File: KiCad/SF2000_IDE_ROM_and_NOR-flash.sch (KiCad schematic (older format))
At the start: 7 parts, among them J5 IDE_ATA_44pin, U13 SST39LF040, U14 SST39LF802C, U15 74LVC245A, U16 74LVC245A, U17 74LVC245A

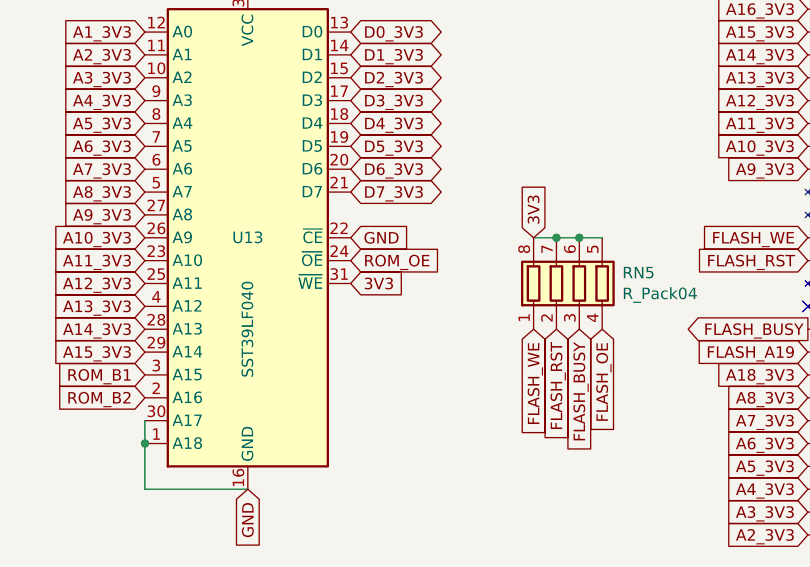
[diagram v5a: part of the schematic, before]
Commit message: added ROM_WE signal/pin to FPGA, removed XRDY-signal/pin, and some silkscreen fixes
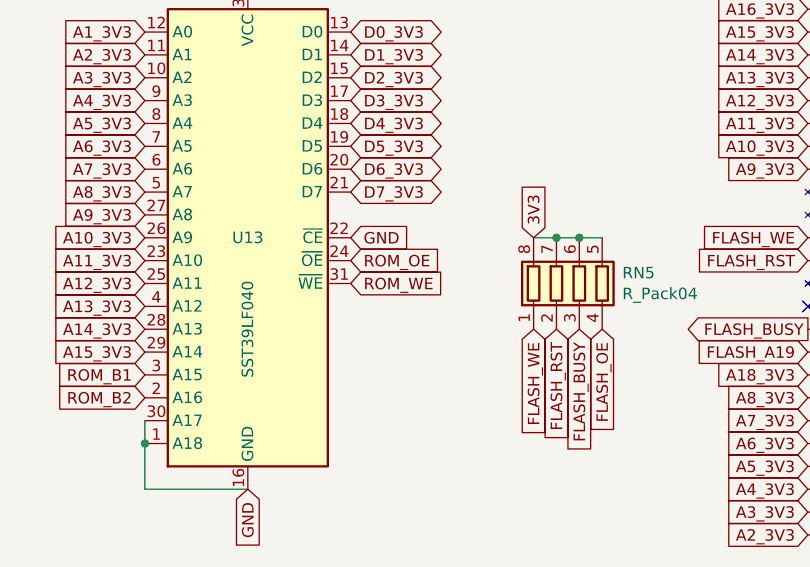
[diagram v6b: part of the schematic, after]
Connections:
- net 3V3: no longer U13.31 (~WE)
- new net ROM_WE: U13.31 (~WE)
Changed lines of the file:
@@
 Wire Wire Line
 	5650 3500 5650 3400
-Text GLabel 6550 2800 2    50   Input ~ 0
-3V3
 NoConn ~ 8550 2900
 $Comp
@@
 Text GLabel 7650 3000 3    50   Input ~ 0
 FLASH_OE
+Text GLabel 6550 2800 2    50   Input ~ 0
+ROM_WE
 $EndSCHEMATC

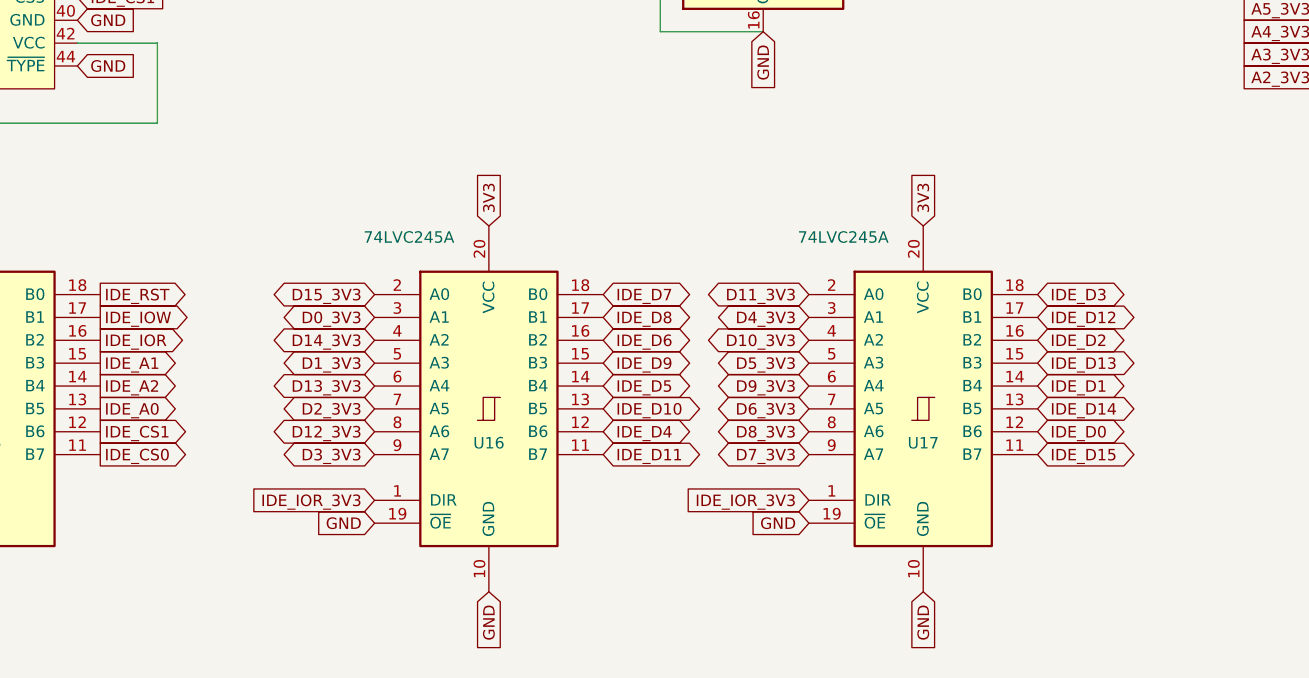
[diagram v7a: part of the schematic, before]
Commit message: added decoupling capacitor for Crystal Oscillator (X1), and some silkcreen fixes/labeling
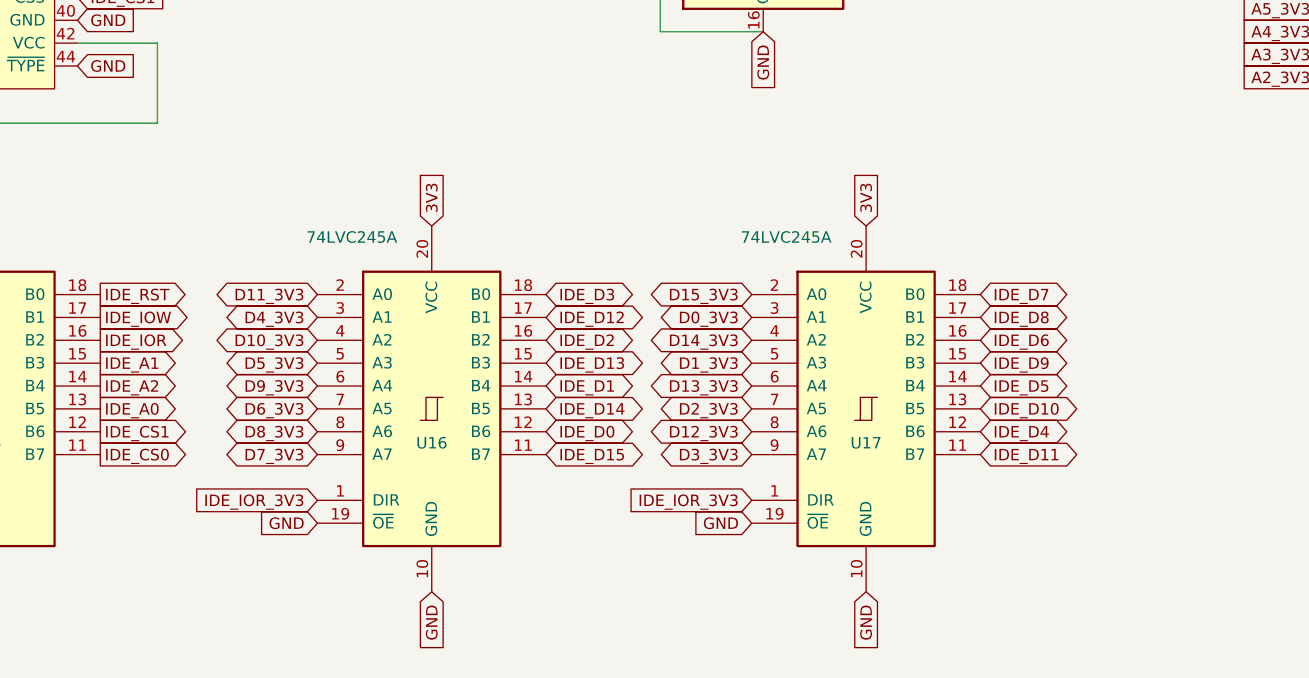
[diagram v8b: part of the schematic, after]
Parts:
- renumbered U17 to U16, U16 to U17
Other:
- moved on the sheet: U16, U17
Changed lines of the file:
@@
 Text GLabel 6550 2400 2    50   BiDi ~ 0
 D7_3V3
-Text GLabel 4400 4950 0    50   BiDi ~ 0
+Text GLabel 6050 4950 0    50   BiDi ~ 0
 D0_3V3
-Text GLabel 4400 5150 0    50   BiDi ~ 0
+Text GLabel 6050 5150 0    50   BiDi ~ 0
 D1_3V3
-Text GLabel 4400 5350 0    50   BiDi ~ 0
+Text GLabel 6050 5350 0    50   BiDi ~ 0
 D2_3V3
-Text GLabel 4400 5550 0    50   BiDi ~ 0
+Text GLabel 6050 5550 0    50   BiDi ~ 0
 D3_3V3
-Text GLabel 6300 4950 0    50   BiDi ~ 0
+Text GLabel 4150 4950 0    50   BiDi ~ 0
 D4_3V3
-Text GLabel 6300 5150 0    50   BiDi ~ 0
+Text GLabel 4150 5150 0    50   BiDi ~ 0
 D5_3V3
-Text GLabel 6300 5350 0    50   BiDi ~ 0
+Text GLabel 4150 5350 0    50   BiDi ~ 0
 D6_3V3
-Text GLabel 6300 5550 0    50   BiDi ~ 0
+Text GLabel 4150 5550 0    50   BiDi ~ 0
 D7_3V3
-Text GLabel 6300 5450 0    50   BiDi ~ 0
+Text GLabel 4150 5450 0    50   BiDi ~ 0
 D8_3V3
-Text GLabel 6300 5250 0    50   BiDi ~ 0
+Text GLabel 4150 5250 0    50   BiDi ~ 0
 D9_3V3
-Text GLabel 6300 5050 0    50   BiDi ~ 0
+Text GLabel 4150 5050 0    50   BiDi ~ 0
 D10_3V3
-Text GLabel 6300 4850 0    50   BiDi ~ 0
+Text GLabel 4150 4850 0    50   BiDi ~ 0
 D11_3V3
-Text GLabel 4400 5450 0    50   BiDi ~ 0
+Text GLabel 6050 5450 0    50   BiDi ~ 0
 D12_3V3
-Text GLabel 4400 5250 0    50   BiDi ~ 0
+Text GLabel 6050 5250 0    50   BiDi ~ 0
 D13_3V3
-Text GLabel 4400 5050 0    50   BiDi ~ 0
+Text GLabel 6050 5050 0    50   BiDi ~ 0
 D14_3V3
-Text GLabel 4400 4850 0    50   BiDi ~ 0
+Text GLabel 6050 4850 0    50   BiDi ~ 0
 D15_3V3
 Text GLabel 2200 4850 0    50   Input ~ 0
@@
 IDE_CS0
 $Comp
-L SF2000:74LVC245A U16
+L SF2000:74LVC245A U17
 U 1 1 628E9EE2
-P 4900 5350
-F 0 "U16" H 4900 5200 50  0000 C CNN
-F 1 "74LVC245A" H 4550 6100 50  0000 C CNN
-F 2 "Package_SO:TSSOP-20_4.4x6.5mm_P0.65mm" H 4900 5350 50  0001 C CNN
-F 3 "http://www.ti.com/lit/gpn/sn74HC245" H 4900 5350 50  0001 C CNN
-	1    4900 5350
+P 6550 5350
+F 0 "U17" H 6550 5200 50  0000 C CNN
+F 1 "74LVC245A" H 6200 6100 50  0000 C CNN
+F 2 "Package_SO:TSSOP-20_4.4x6.5mm_P0.65mm" H 6550 5350 50  0001 C CNN
+F 3 "http://www.ti.com/lit/gpn/sn74HC245" H 6550 5350 50  0001 C CNN
+	1    6550 5350
 	1    0    0    -1
 $EndComp
-Text GLabel 4900 4550 1    50   Input ~ 0
-3V3
-Text GLabel 4900 6150 3    50   Input ~ 0
-GND
-Text GLabel 4400 5850 0    50   Input ~ 0
+Text GLabel 6550 4550 1    50   Input ~ 0
+3V3
+Text GLabel 6550 6150 3    50   Input ~ 0
+GND
+Text GLabel 6050 5850 0    50   Input ~ 0
 GND
 $Comp
-L SF2000:74LVC245A U17
+L SF2000:74LVC245A U16
 U 1 1 628ED6C8
-P 6800 5350
-F 0 "U17" H 6800 5200 50  0000 C CNN
-F 1 "74LVC245A" H 6450 6100 50  0000 C CNN
-F 2 "Package_SO:TSSOP-20_4.4x6.5mm_P0.65mm" H 6800 5350 50  0001 C CNN
-F 3 "http://www.ti.com/lit/gpn/sn74HC245" H 6800 5350 50  0001 C CNN
-	1    6800 5350
+P 4650 5350
+F 0 "U16" H 4650 5200 50  0000 C CNN
+F 1 "74LVC245A" H 4300 6100 50  0000 C CNN
+F 2 "Package_SO:TSSOP-20_4.4x6.5mm_P0.65mm" H 4650 5350 50  0001 C CNN
+F 3 "http://www.ti.com/lit/gpn/sn74HC245" H 4650 5350 50  0001 C CNN
+	1    4650 5350
 	1    0    0    -1
 $EndComp
-Text GLabel 6800 4550 1    50   Input ~ 0
-3V3
-Text GLabel 6800 6150 3    50   Input ~ 0
-GND
-Text GLabel 6300 5850 0    50   Input ~ 0
-GND
-Text GLabel 6300 5750 0    50   Input ~ 0
+Text GLabel 4650 4550 1    50   Input ~ 0
+3V3
+Text GLabel 4650 6150 3    50   Input ~ 0
+GND
+Text GLabel 4150 5850 0    50   Input ~ 0
+GND
+Text GLabel 4150 5750 0    50   Input ~ 0
 IDE_IOR_3V3
-Text GLabel 4400 5750 0    50   Input ~ 0
+Text GLabel 6050 5750 0    50   Input ~ 0
 IDE_IOR_3V3
-Text GLabel 5400 4850 2    50   BiDi ~ 0
+Text GLabel 7050 4850 2    50   BiDi ~ 0
 IDE_D7
 Text GLabel 2300 1850 0    50   BiDi ~ 0
 IDE_D7
-Text GLabel 5400 4950 2    50   BiDi ~ 0
+Text GLabel 7050 4950 2    50   BiDi ~ 0
 IDE_D8
 Text GLabel 3100 1850 2    50   BiDi ~ 0
 IDE_D8
-Text GLabel 5400 5050 2    50   BiDi ~ 0
+Text GLabel 7050 5050 2    50   BiDi ~ 0
 IDE_D6
 Text GLabel 2300 1950 0    50   BiDi ~ 0
 IDE_D6
-Text GLabel 5400 5150 2    50   BiDi ~ 0
+Text GLabel 7050 5150 2    50   BiDi ~ 0
 IDE_D9
 Text GLabel 3100 1950 2    50   BiDi ~ 0
 IDE_D9
-Text GLabel 5400 5250 2    50   BiDi ~ 0
+Text GLabel 7050 5250 2    50   BiDi ~ 0
 IDE_D5
 Text GLabel 2300 2050 0    50   BiDi ~ 0
 IDE_D5
-Text GLabel 5400 5350 2    50   BiDi ~ 0
+Text GLabel 7050 5350 2    50   BiDi ~ 0
 IDE_D10
 Text GLabel 3100 2050 2    50   BiDi ~ 0
 IDE_D10
-Text GLabel 5400 5450 2    50   BiDi ~ 0
+Text GLabel 7050 5450 2    50   BiDi ~ 0
 IDE_D4
 Text GLabel 2300 2150 0    50   BiDi ~ 0
 IDE_D4
-Text GLabel 5400 5550 2    50   BiDi ~ 0
+Text GLabel 7050 5550 2    50   BiDi ~ 0
 IDE_D11
 Text GLabel 3100 2150 2    50   BiDi ~ 0
 IDE_D11
-Text GLabel 7300 4850 2    50   BiDi ~ 0
+Text GLabel 5150 4850 2    50   BiDi ~ 0
 IDE_D3
 Text GLabel 2300 2250 0    50   BiDi ~ 0
 IDE_D3
-Text GLabel 7300 4950 2    50   BiDi ~ 0
+Text GLabel 5150 4950 2    50   BiDi ~ 0
 IDE_D12
 Text GLabel 3100 2250 2    50   BiDi ~ 0
 IDE_D12
-Text GLabel 7300 5050 2    50   BiDi ~ 0
+Text GLabel 5150 5050 2    50   BiDi ~ 0
 IDE_D2
 Text GLabel 2300 2350 0    50   BiDi ~ 0
 IDE_D2
-Text GLabel 7300 5150 2    50   BiDi ~ 0
+Text GLabel 5150 5150 2    50   BiDi ~ 0
 IDE_D13
 Text GLabel 3100 2350 2    50   BiDi ~ 0
 IDE_D13
-Text GLabel 7300 5250 2    50   BiDi ~ 0
+Text GLabel 5150 5250 2    50   BiDi ~ 0
 IDE_D1
 Text GLabel 2300 2450 0    50   BiDi ~ 0
 IDE_D1
-Text GLabel 7300 5350 2    50   BiDi ~ 0
+Text GLabel 5150 5350 2    50   BiDi ~ 0
 IDE_D14
 Text GLabel 3100 2450 2    50   BiDi ~ 0
 IDE_D14
-Text GLabel 7300 5450 2    50   BiDi ~ 0
+Text GLabel 5150 5450 2    50   BiDi ~ 0
 IDE_D0
 Text GLabel 2300 2550 0    50   BiDi ~ 0
 IDE_D0
-Text GLabel 7300 5550 2    50   BiDi ~ 0
+Text GLabel 5150 5550 2    50   BiDi ~ 0
 IDE_D15
 Text GLabel 3100 2550 2    50   BiDi ~ 0
